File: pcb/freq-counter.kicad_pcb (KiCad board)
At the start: 4 copper layers, 152.4 x 167.6 mm, 107 parts, among them J1 RPM on board, J10 Power_T1, J11 Hz/RPM_Terminal1, J12 Hz/RPM_Terminal0, J13 1kMG_Terminal1, J14 1kMG_Terminal0, J2 BNC, J3 RPM to Board, J4 Jack-DC, J5 Segments-Terminal0, J6 Digits-Terminal0, J7 Segments-Terminal1, J8 Digits-Terminal1, J9 Power_Terminal1, Q1 CSC388A, Q10 2SC1815, Q11 2SC1815, Q12 2SC1815, Q13 2SC1815, Q14 2SC1815, Q2 CSC388A, Q3 2SA1015, Q4 2SC1815, Q5 2SC1815, Q6 CSC388A, Q7 CSC388A, Q8 CSC388A, Q9 2SC1815, SW1 on/off, SW2 count up, SW3 toggle, SW4 SW_SIGNAL, U1 SN74HC02N, U2 ATTINY4313-PU(freq-counter), U3 EE-SX460, U4 74HC00, U5 74HC00, U6 74HC00, U7 7seg-2digit-ca, U8 7seg-2digit-ca, U9 7seg-2digit-ca, Y1 10MHz

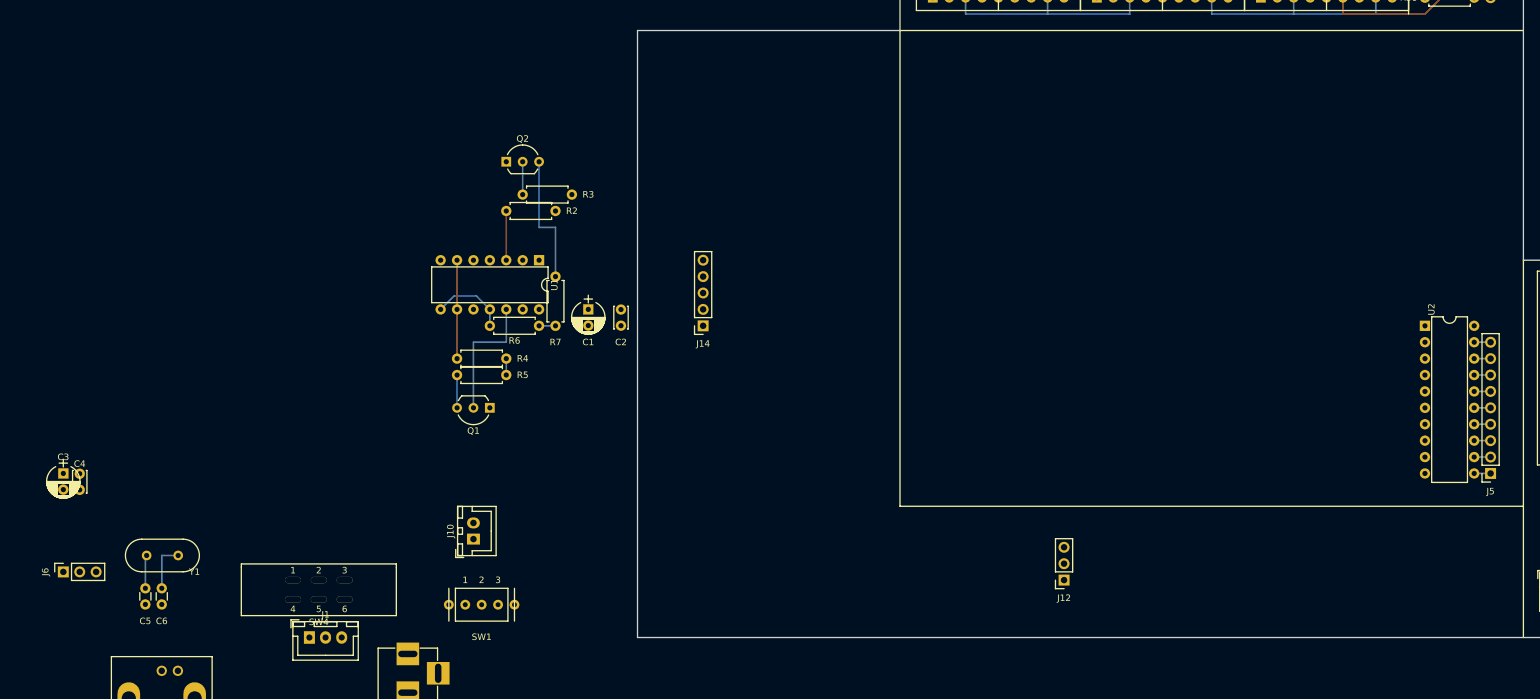
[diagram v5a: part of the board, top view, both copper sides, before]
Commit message: Terminal0 系を配置。
後は上手く配線をするだけ。
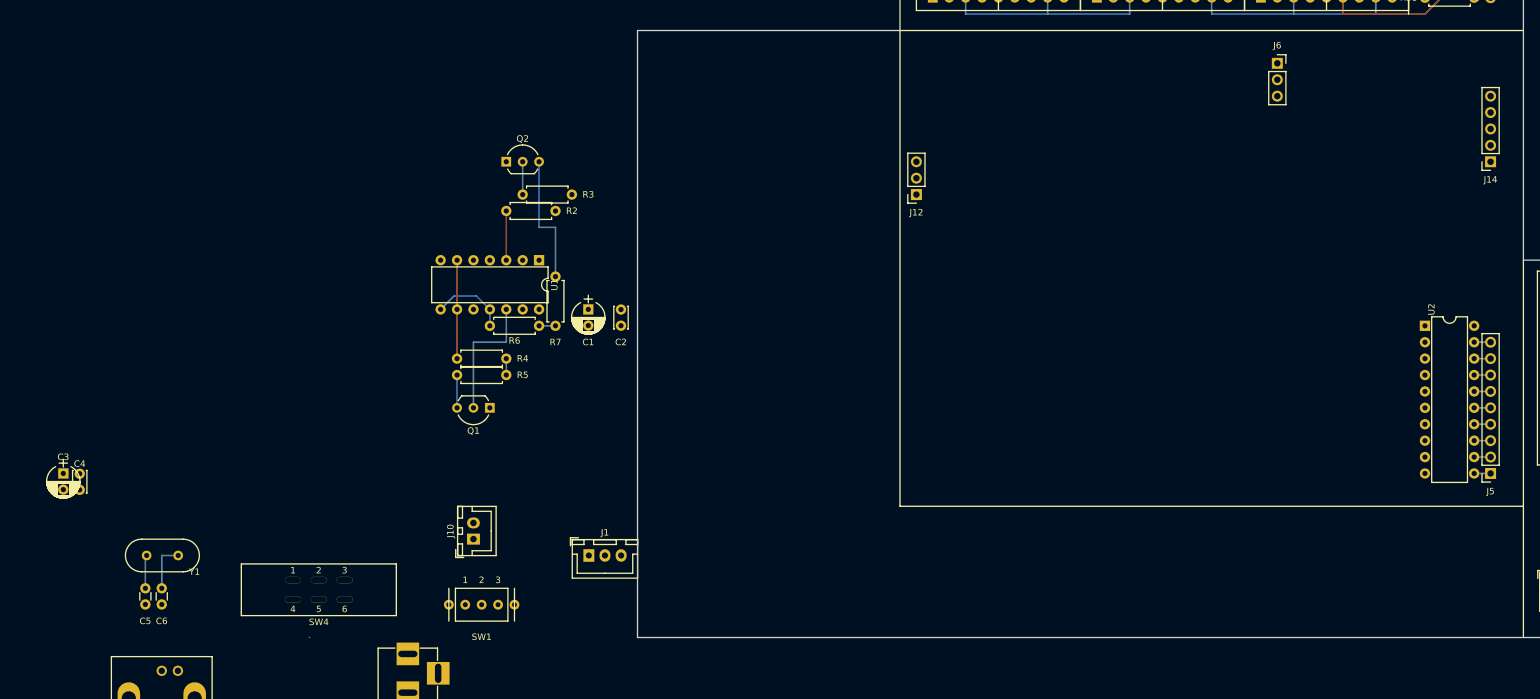
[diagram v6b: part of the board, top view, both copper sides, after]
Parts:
- J10: value Power_T1 -> Power-Terminal0
- J9: value Power_Terminal1 -> Power-Terminal1
- moved J6 203.8 mm to (142.2, 109.2), turned to 0 degrees
- moved J14 124.5 mm to (175.3, 124.5)
- moved J12 63.9 mm to (86.4, 129.5)
- moved J1 45.1 mm to (35.6, 185.4)
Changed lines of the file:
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@@
   (general
     (links 262)
-    (no_connects 70)
+    (no_connects 68)
     (area 43.104999 30.40317 195.655012 198.195006)
     (thickness 1.6)
@@
   )
   (module Conn_JST:JST_XH_B03B-XH-A_1x03_P2.50mm_Horizontal (layer F.Cu)
-    (at -7.62 198.12)
+    (at 35.64 185.42)
     (descr "JST XH series connector, B03B-XH-A (http://www.jst-mfg.com/product/pdf/eng/eXH.pdf), generated with kicad-footprint-generator")
     (tags "connector JST XH top entry")
@@
       (effects (font (size 1 1) (thickness 0.15)))
     )
-    (fp_text value Power_Terminal1 (at 1.25 4.6 180) (layer F.Fab)
+    (fp_text value Power-Terminal1 (at 1.25 4.6 180) (layer F.Fab)
       (effects (font (size 1 1) (thickness 0.15)))
     )
@@
       (effects (font (size 1 1) (thickness 0.15)))
     )
-    (fp_text value Power_T1 (at 1.25 4.6 90) (layer F.Fab)
+    (fp_text value Power-Terminal0 (at 1.25 4.6 90) (layer F.Fab)
       (effects (font (size 1 1) (thickness 0.15)))
     )
@@
   )
   (module Connector_PinSocket_2.54mm:PinSocket_1x03_P2.54mm_Vertical (layer F.Cu)
-    (at -45.72 187.96 90)
+    (at 142.24 109.22)
     (descr "Through hole straight socket strip, 1x03, 2.54mm pitch, single row (from Kicad 4.0.7), script generated")
     (tags "Through hole socket strip THT 1x03 2.54mm single row")
-    (fp_text reference J6 (at 0 -2.77 90) (layer F.SilkS)
+    (fp_text reference J6 (at 0 -2.77) (layer F.SilkS)
       (effects (font (size 1 1) (thickness 0.15)))
     )
-    (fp_text value Digits-Terminal0 (at 0 7.85 90) (layer F.Fab)
+    (fp_text value Digits-Terminal0 (at 0 7.85) (layer F.Fab)
       (effects (font (size 1 1) (thickness 0.15)))
     )
@@
     (fp_line (start 1.75 6.85) (end -1.8 6.85) (layer F.CrtYd) (width 0.05))
     (fp_line (start -1.8 6.85) (end -1.8 -1.8) (layer F.CrtYd) (width 0.05))
-    (fp_text user %R (at 0 2.54 180) (layer F.Fab)
+    (fp_text user %R (at 0 2.54 90) (layer F.Fab)
       (effects (font (size 1 1) (thickness 0.15)))
     )
-    (pad 1 thru_hole rect (at 0 0 90) (size 1.7 1.7) (drill 1) (layers *.Cu *.Mask)
+    (pad 1 thru_hole rect (at 0 0) (size 1.7 1.7) (drill 1) (layers *.Cu *.Mask)
       (net 86 "Net-(J6-Pad1)"))
-    (pad 2 thru_hole oval (at 0 2.54 90) (size 1.7 1.7) (drill 1) (layers *.Cu *.Mask)
+    (pad 2 thru_hole oval (at 0 2.54) (size 1.7 1.7) (drill 1) (layers *.Cu *.Mask)
       (net 87 "Net-(J6-Pad2)"))
-    (pad 3 thru_hole oval (at 0 5.08 90) (size 1.7 1.7) (drill 1) (layers *.Cu *.Mask)
+    (pad 3 thru_hole oval (at 0 5.08) (size 1.7 1.7) (drill 1) (layers *.Cu *.Mask)
       (net 88 "Net-(J6-Pad3)"))
     (model ${KISYS3DMOD}/Connector_PinSocket_2.54mm.3dshapes/PinSocket_1x03_P2.54mm_Vertical.wrl
@@
   )
   (module Connector_PinSocket_2.54mm:PinSocket_1x03_P2.54mm_Vertical (layer F.Cu)
-    (at 109.22 189.23 180)
+    (at 86.36 129.54 180)
     (descr "Through hole straight socket strip, 1x03, 2.54mm pitch, single row (from Kicad 4.0.7), script generated")
     (tags "Through hole socket strip THT 1x03 2.54mm single row")
@@
   )
   (module Connector_PinSocket_2.54mm:PinSocket_1x05_P2.54mm_Vertical (layer F.Cu)
-    (at 53.34 149.86 180)
+    (at 175.26 124.46 180)
     (descr "Through hole straight socket strip, 1x05, 2.54mm pitch, single row (from Kicad 4.0.7), script generated")
     (tags "Through hole socket strip THT 1x05 2.54mm single row")

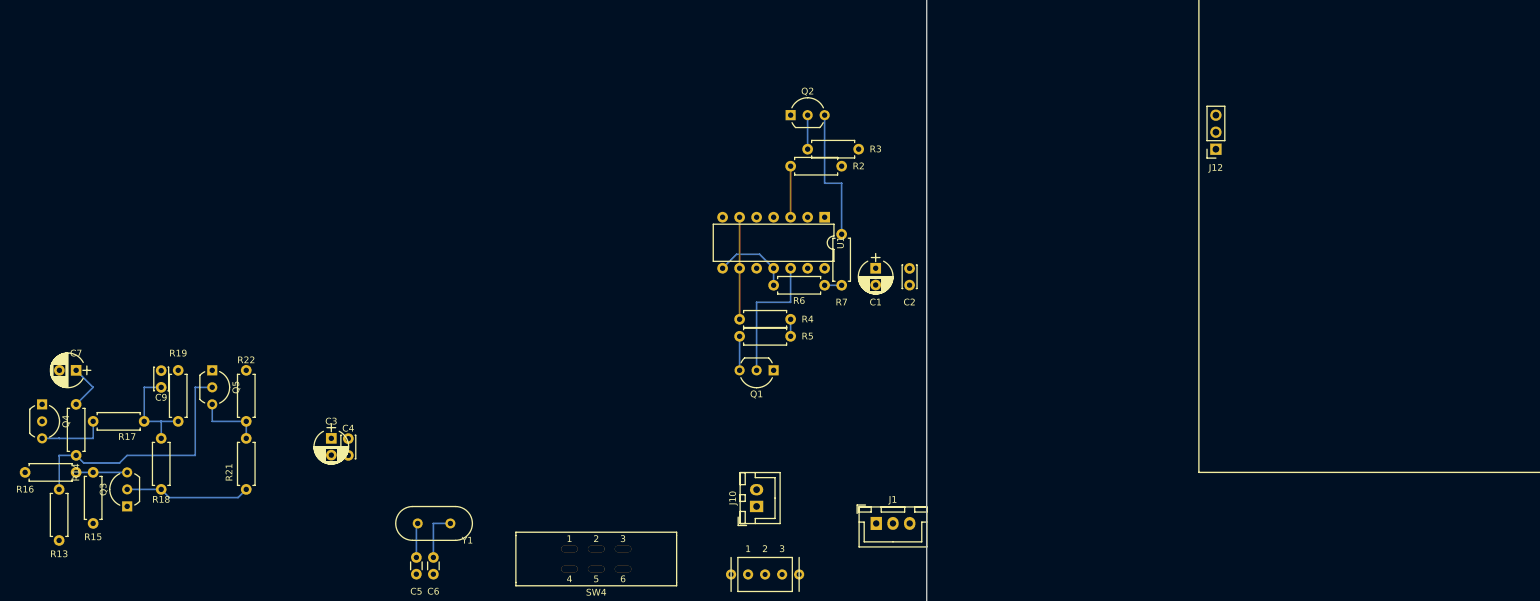
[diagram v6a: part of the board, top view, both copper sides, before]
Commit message: Terminal0系をlock。 Hz/RPMの部品をHz/RPM-Terminal0付近に配置。
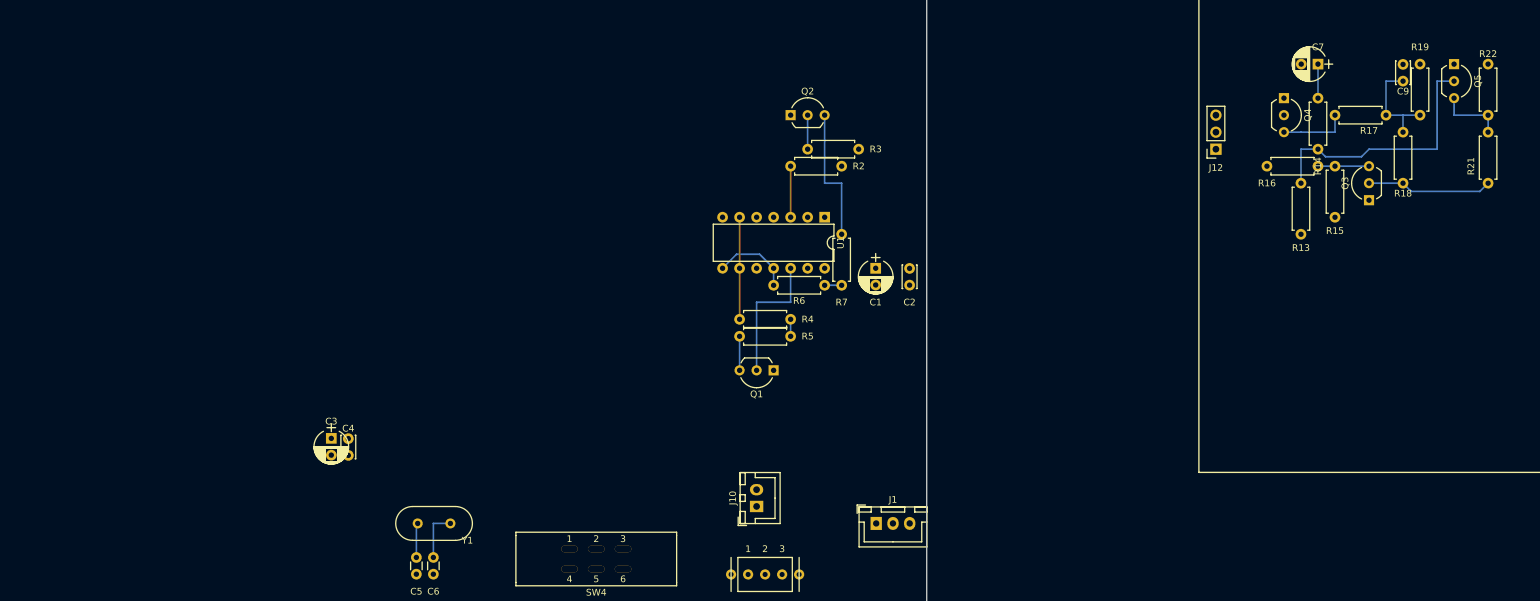
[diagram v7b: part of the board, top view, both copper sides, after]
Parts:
- moved C9 191.0 mm to (114.3, 116.9)
- moved Q3 191.0 mm to (109.2, 137.2)
- moved Q4 191.0 mm to (96.5, 121.9)
- moved R13 191.0 mm to (99.1, 134.6)
- moved R15 191.0 mm to (104.1, 132.1)
- moved R16 191.0 mm to (94.0, 132.1)
- moved R18 191.0 mm to (114.3, 127.0)
- moved R21 191.0 mm to (127.0, 127.0)
- moved C7 191.0 mm to (101.6, 116.8)
- moved Q5 191.0 mm to (121.9, 116.8)
- moved R17 191.0 mm to (111.8, 124.5)
- moved R19 191.0 mm to (116.8, 116.8)
- moved R22 191.0 mm to (127.0, 116.8)
- moved R14 191.0 mm to (101.6, 121.9)
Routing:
- net /TOGGLE0_T0: track 7.18 -> 5.08 mm

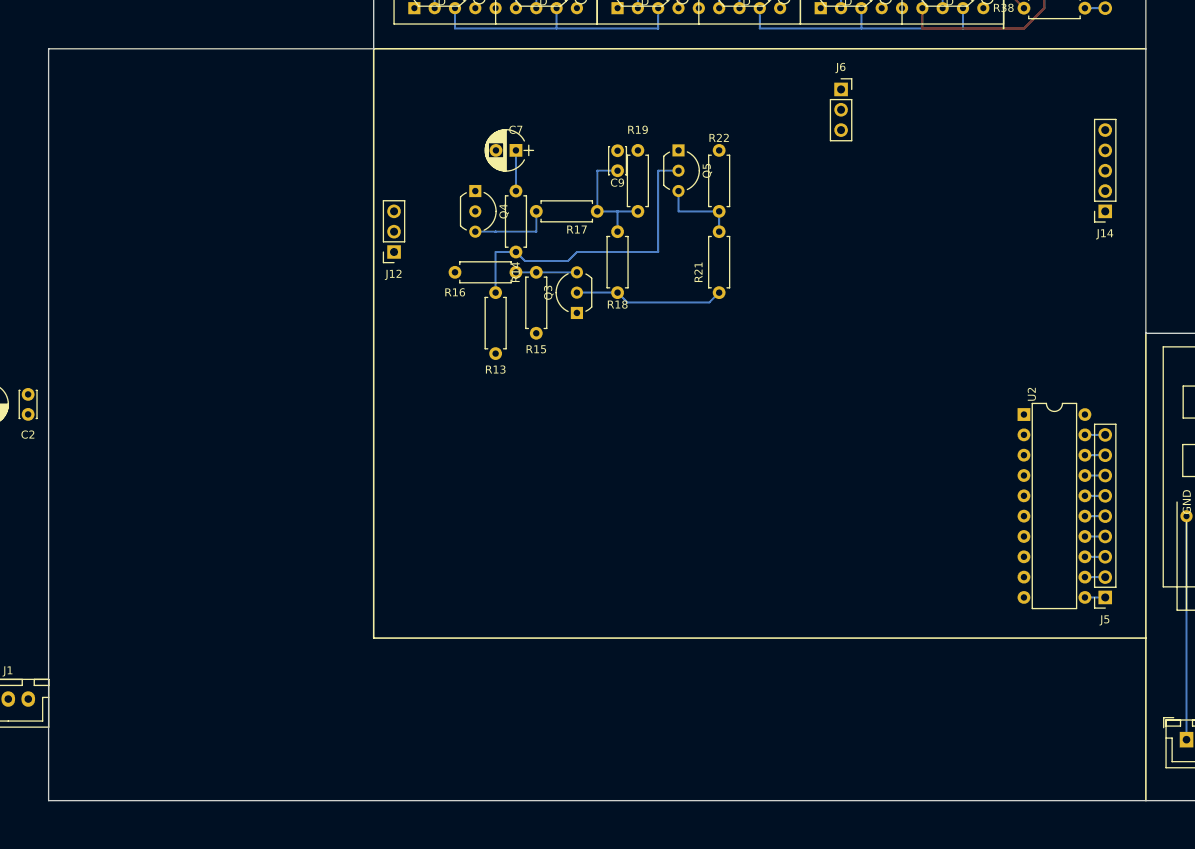
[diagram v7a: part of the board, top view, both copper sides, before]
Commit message: 基板外形を決定。Terminal0の位置も決定し，Lockしておいた。
なんとか上手く２階建てにできそう。
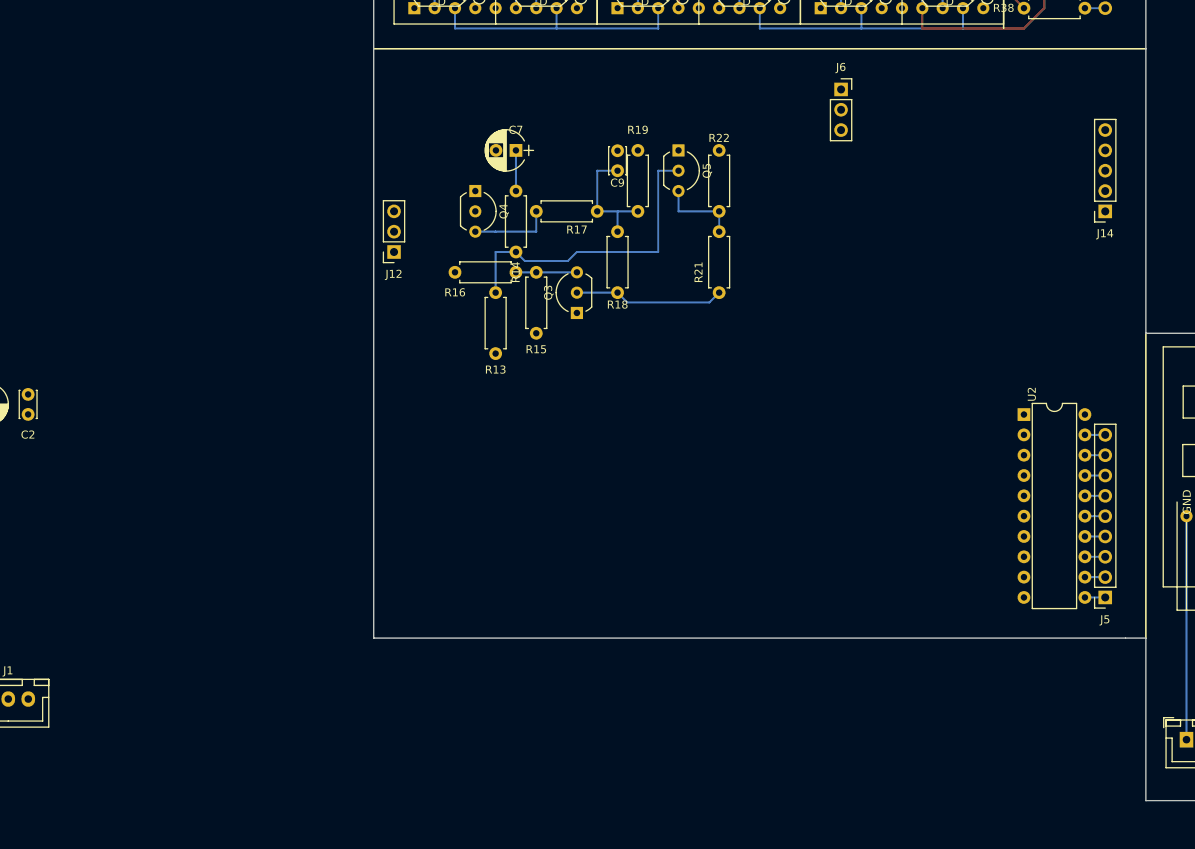
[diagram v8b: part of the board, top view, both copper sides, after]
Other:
- board size 152.4 x 167.6 mm -> 111.8 x 167.6 mm
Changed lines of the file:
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@@
     (area 43.104999 30.40317 195.655012 198.195006)
     (thickness 1.6)
-    (drawings 36)
+    (drawings 35)
     (tracks 482)
     (zones 0)
@@
     )
   )
+  (gr_line (start 180.34 177.8) (end 180.34 139.7) (layer F.SilkS) (width 0.2))
+  (gr_line (start 180.34 177.8) (end 180.34 198.12) (layer Edge.Cuts) (width 0.15))
+  (gr_line (start 177.8 177.8) (end 180.34 177.8) (layer Edge.Cuts) (width 0.15))
+  (gr_line (start 83.82 177.8) (end 177.8 177.8) (layer Edge.Cuts) (width 0.15))
+  (gr_line (start 83.82 104.14) (end 83.82 177.8) (layer Edge.Cuts) (width 0.15))
   (gr_text RPM (at 95.25 40.64) (layer F.SilkS)
     (effects (font (size 1.5 1.5) (thickness 0.3)))
   )
   (gr_line (start 162.56 71.12) (end 175.26 71.12) (layer F.SilkS) (width 0.2))
-  (gr_line (start 83.82 177.8) (end 83.82 104.14) (layer F.SilkS) (width 0.2))
-  (gr_line (start 180.34 177.8) (end 83.82 177.8) (layer F.SilkS) (width 0.2))
   (gr_line (start 83.82 104.14) (end 180.34 104.14) (layer F.SilkS) (width 0.2))
-  (gr_line (start 83.82 104.14) (end 43.18 104.14) (layer Edge.Cuts) (width 0.15))
   (gr_line (start 180.34 30.48) (end 180.34 104.14) (layer Edge.Cuts) (width 0.15))
   (gr_line (start 83.81999 30.478171) (end 83.81999 104.138171) (layer Edge.Cuts) (width 0.15))
@@
   )
   (gr_line (start 180.34 104.14) (end 180.34 139.7) (layer Edge.Cuts) (width 0.15))
-  (gr_line (start 43.18 198.12) (end 43.18 104.14) (layer Edge.Cuts) (width 0.15))
   (gr_text Bit2 (at 147.320001 40.639994) (layer F.SilkS)
     (effects (font (size 1.5 1.5) (thickness 0.3)))
@@
     (effects (font (size 1.5 1.5) (thickness 0.3)))
   )
-  (gr_line (start 180.34 139.7) (end 180.34 198.12) (layer F.SilkS) (width 0.2))
-  (gr_line (start 180.34 198.12) (end 43.18 198.12) (layer Edge.Cuts) (width 0.15))
   (gr_line (start 180.340011 139.700005) (end 195.580011 139.700005) (layer Edge.Cuts) (width 0.15))
   (gr_line (start 195.580011 198.120005) (end 180.340011 198.120005) (layer Edge.Cuts) (width 0.15))
